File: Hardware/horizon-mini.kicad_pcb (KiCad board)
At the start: 2 copper layers, 34 x 34 mm, 79 parts, among them J2 Conn_01x02_Pin, J3 Micro_SD_Card_Det1, J7 USB_C_Receptacle_USB2.0_16P, J8 Conn_02x03_Counter_Clockwise, Q10 DMG2301L, U1 TPS82130, U16 AP2112K-3.3, U2 TPS61092, U3 LTC4412xS6, U5 ATSAMD21G18A-A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

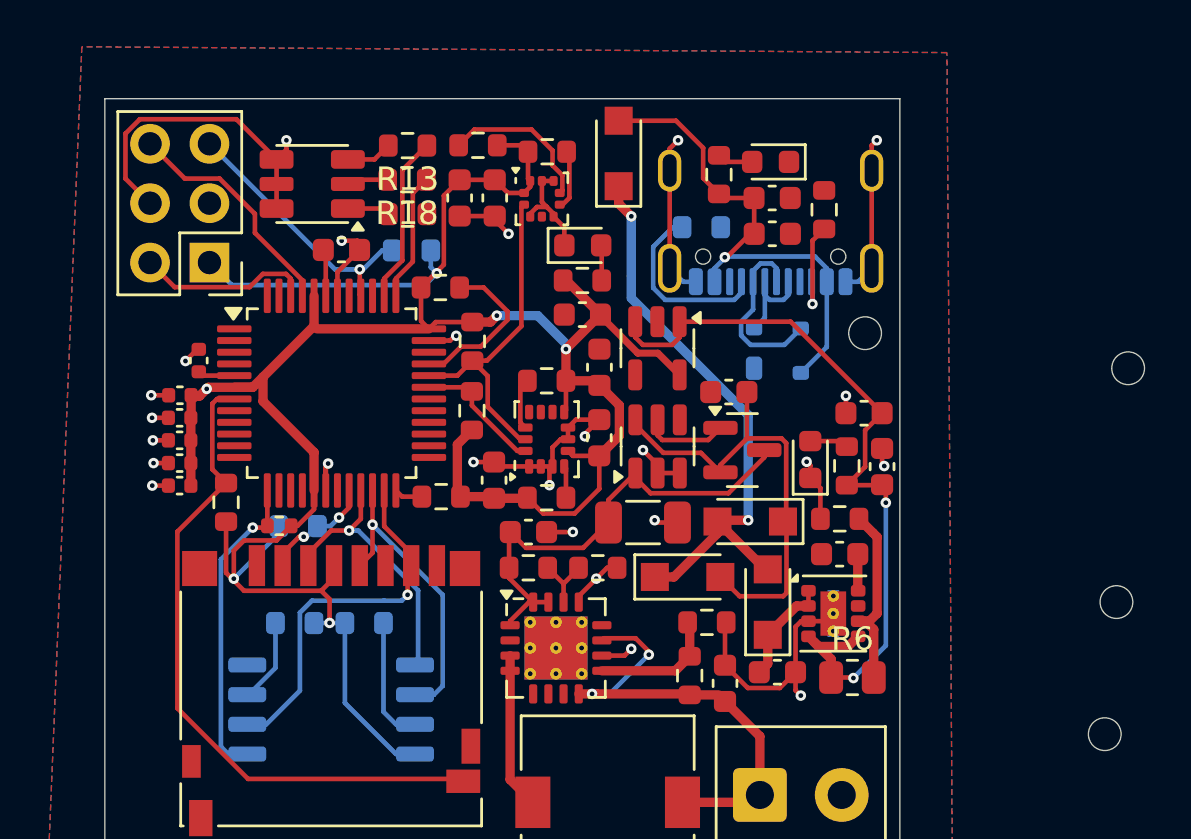
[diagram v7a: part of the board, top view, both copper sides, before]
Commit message: routing v2 should be done
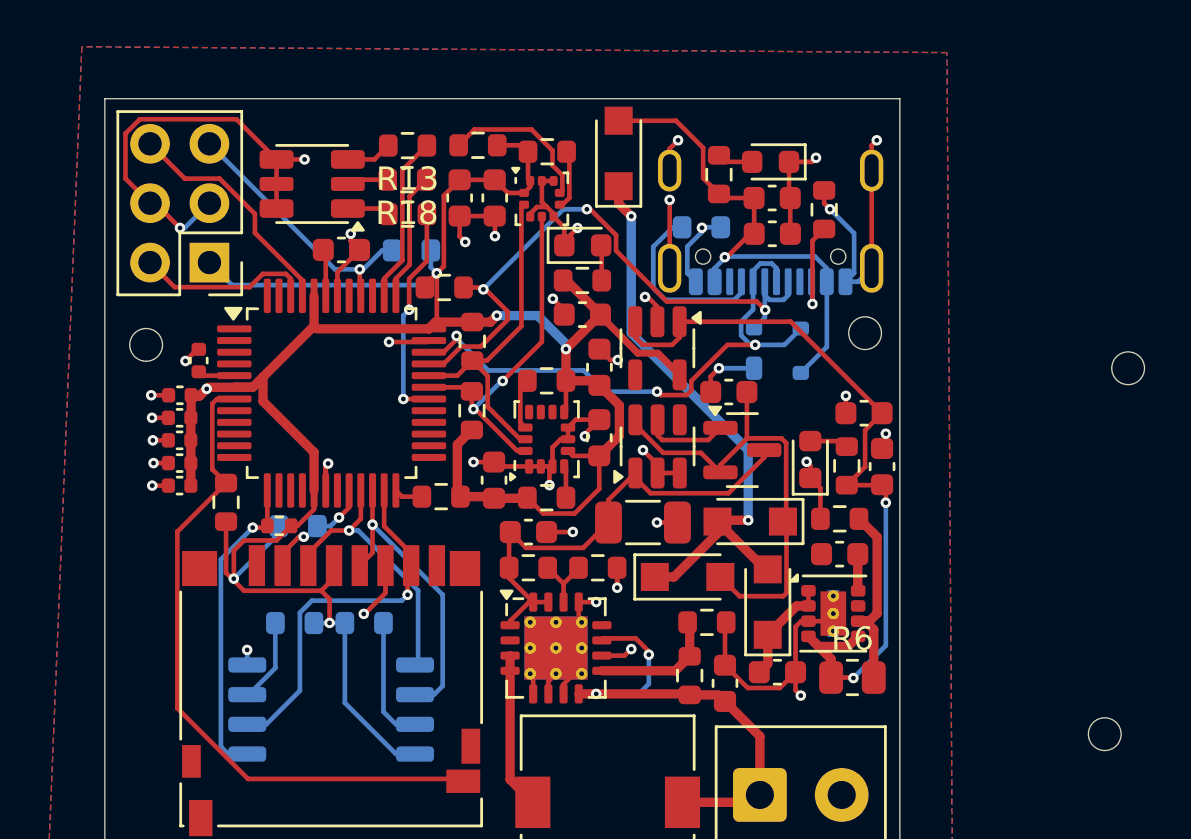
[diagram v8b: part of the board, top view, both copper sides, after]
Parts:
- moved REF** 42.9 mm to (137.8, 113.0)
- moved R27 0.17 mm to (150.5, 110.5)
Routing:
- net GND: track 77.7 -> 105.7 mm, vias 25 -> 39
- net D- DMCU-2: track 7.77 -> 25.0 mm, vias 0 -> 3
- net D+ DMCU-2: track 11.5 -> 27.1 mm, vias 0 -> 3
- net I2C0_SDA: track 5.60 -> 15.1 mm, vias 0 -> 2
- net 2B: track 0.00 -> 9.43 mm, vias 0 -> 2
- net Net-(J2-Pin_1): track 20.2 -> 20.9 mm
- net +3.3V: track 111.7 -> 112.3 mm
